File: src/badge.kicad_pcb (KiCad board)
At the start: 2 copper layers, 52.5 x 84.8 mm, 974 parts, among them J1 Conn_01x25_Male, U1 PROTO_SOIC6, U10 PROTO_SOT23, U100 PAD, U1001 PAD, U101 PAD, U102 PAD, U103 PAD, U104 PAD, U105 PAD, U106 PAD, U107 PAD, U108 PAD, U109 PAD, U11 PROTO_SOIC6, U110 PAD, U111 PAD, U112 PAD, U113 PAD, U114 PAD, U115 PAD, U116 PAD, U117 PAD, U118 PAD, U119 PAD, U12 PROTO_SOT23, U120 PAD, U121 PAD, U122 PAD, U123 PAD, U124 PAD, U125 PAD, U126 PAD, U127 PAD, U128 PAD, U129 PAD, U13 PROTO_SOIC6, U130 PAD, U131 PAD, U132 PAD, U133 PAD, U134 PAD, U135 PAD, U136 PAD, U137 PAD, U138 PAD, U139 PAD, U14 PROTO_SOT23, U140 PAD, U141 PAD, U142 PAD, U143 PAD, U144 PAD, U145 PAD, U146 PAD, U147 PAD, U148 PAD, U149 PAD, U15 PROTO_SOIC6, U150 PAD, U151 PAD, U152 PAD, U153 PAD, U154 PAD, U155 PAD, U156 PAD, U157 PAD, U158 PAD, U159 PAD, U16 PROTO_SOT23, U160 PAD, U161 PAD, U162 PAD, U163 PAD, U164 PAD, U165 PAD, U166 PAD, U167 PAD, U168 PAD, U169 PAD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

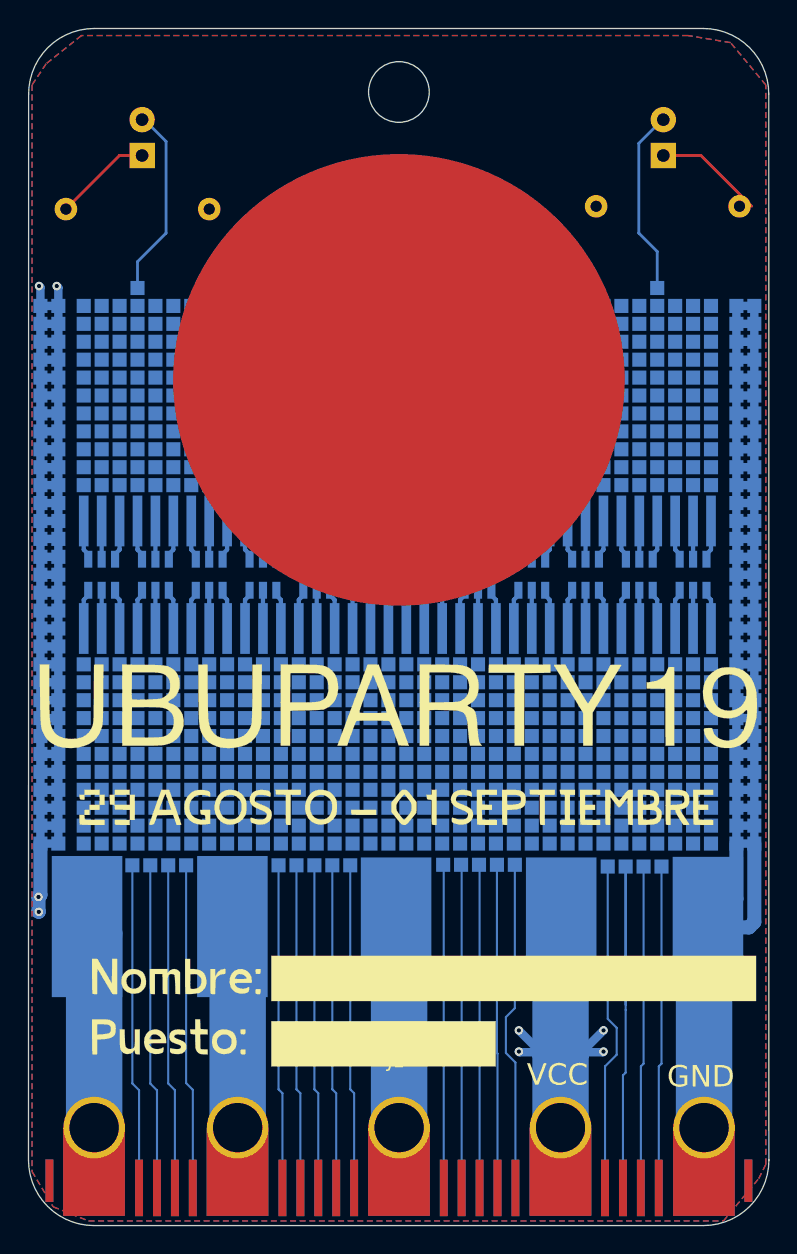
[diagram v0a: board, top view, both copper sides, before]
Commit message: Added Version 24 and 25 of the badge
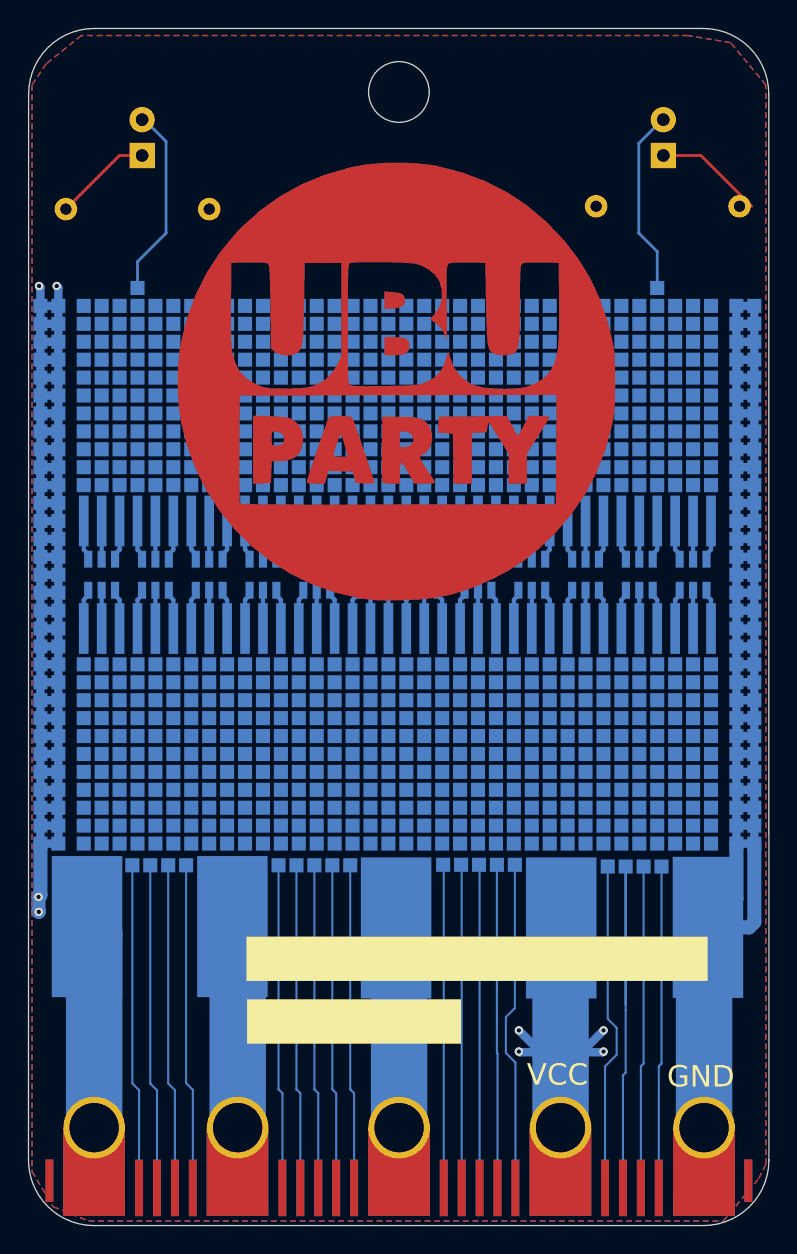
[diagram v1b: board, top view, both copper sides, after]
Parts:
- removed the G*** at (72.0, 109.2)
- removed the G*** at (72.0, 75.0)
- added ?: , , F.Cu at (66.8, 117.6)
- added ?: , , F.Cu at (71.3, 103.4)
- added ?: , , F.Cu at (71.6, 75.2)
